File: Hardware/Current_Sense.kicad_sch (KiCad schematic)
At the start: 39 parts, among them IC2 INA241A4IDR, IC3 AMC1350DWVR, J6 Scrut Conn, SW4 Scrut Select, U10 TLV9002QDRQ1, U9 REF35125QDBVR

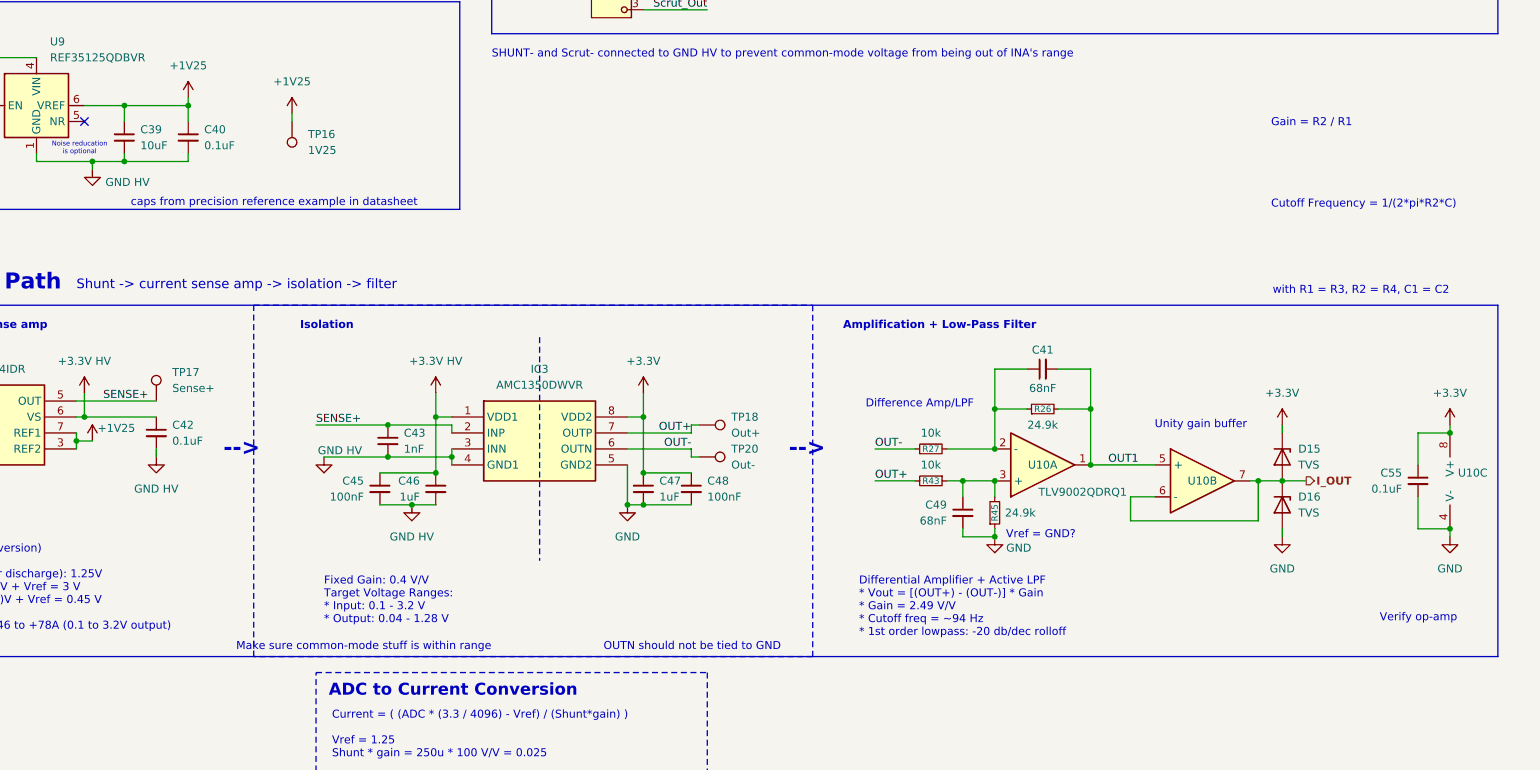
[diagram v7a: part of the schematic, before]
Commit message: refactored and added LPF docs; added fuse, boot_gpio from USB-UART chip
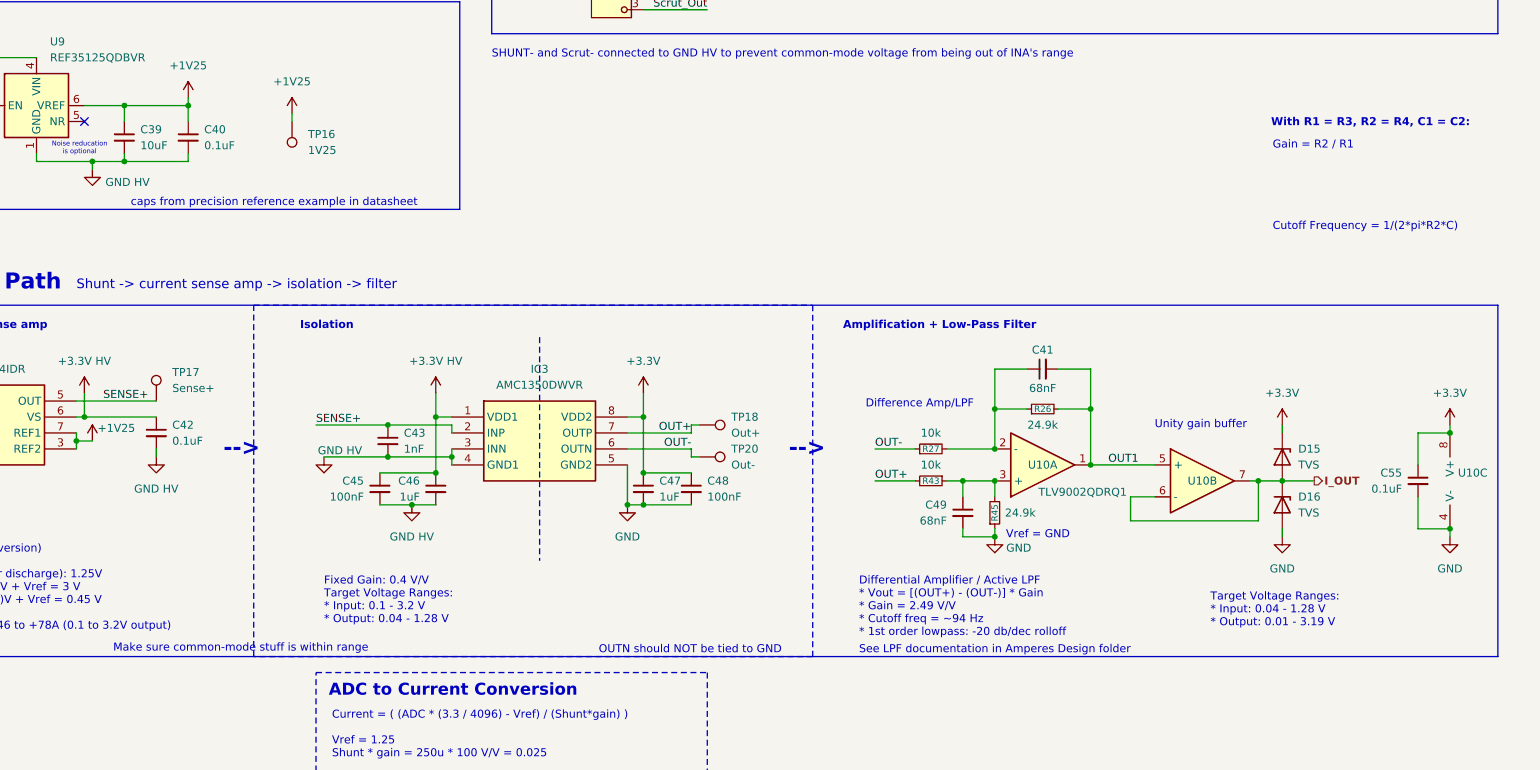
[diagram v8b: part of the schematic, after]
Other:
- note added: "Differential Amplifier / Active LPF * Vout = [(OUT+) - (OUT-)] * Gain * Gain = 2.49 V/V * Cutoff freq = ~94 Hz * 1st order lowpass: -20 db/dec rolloff"
- note added: "OUTN should NOT be tied to GND"
- note added: "See LPF documentation in Amperes Design folder"
- note added: "Target Voltage Ranges: * Input: 0.04 - 1.28 V * Output: 0.01 - 3.19 V"
- note added: "Vref = GND"
- note added: "With R1 = R3, R2 = R4, C1 = C2:"
- note removed: "Differential Amplifier + Active LPF * Vout = [(OUT+) - (OUT-)] * Gain * Gain = 2.49 V/V * Cutoff freq = ~94 Hz * 1st order lowpass: -20 db/dec rolloff"
- note removed: "OUTN should not be tied to GND"
- note removed: "Verify op-amp"
- note removed: "Vref = GND?"
- note removed: "with R1 = R3, R2 = R4, C1 = C2"
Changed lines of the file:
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@@
 		)
 	)
+	(text "Target Voltage Ranges:\n* Input: 0.04 - 1.28 V\n* Output: 0.01 - 3.19 V"
+		(exclude_from_sim no)
+		(at 236.22 152.4 0)
+		(effects
+			(font
+				(size 1.27 1.27)
+			)
+			(justify left top)
+		)
+	)
 	(text "Input"
 		(exclude_from_sim no)
@@
 	(text "Make sure common-mode stuff is within range"
 		(exclude_from_sim no)
-		(at 81.28 160.274 0)
+		(at 61.722 160.528 0)
 		(effects
 			(font
@@
 		)
 	)
-	(text "Verify op-amp"
+	(text "Current = ( (ADC * (3.3 / 4096) - Vref) / (Shunt*gain) )\n\nVref = 1.25\nShunt * gain = 250u * 100 V/V = 0.025\n"
 		(exclude_from_sim no)
-		(at 263.144 155.702 0)
+		(at 96.52 171.196 0)
 		(effects
 			(font
 				(size 1.27 1.27)
-				(color 255 8 29 1)
 			)
 			(justify left top)
 		)
 	)
-	(text "Current = ( (ADC * (3.3 / 4096) - Vref) / (Shunt*gain) )\n\nVref = 1.25\nShunt * gain = 250u * 100 V/V = 0.025\n"
+	(text "Difference Amp/LPF"
 		(exclude_from_sim no)
-		(at 96.52 171.196 0)
+		(at 189.992 122.428 0)
 		(effects
 			(font
 				(size 1.27 1.27)
 			)
-			(justify left top)
 		)
 	)
-	(text "Difference Amp/LPF"
+	(text "Gain: 100 V/V\nRsense = 250 uOhm\nPsense = Rsense * (70A)^2 = 1.225 W\n\nPicked shunt first, then adjusted gain to meet ADC range\nIf additional gain is needed, tweak filter circuit"
 		(exclude_from_sim no)
-		(at 189.992 122.428 0)
+		(at 16.256 183.134 0)
 		(effects
 			(font
 				(size 1.27 1.27)
 			)
+			(justify left top)
 		)
 	)
-	(text "Gain: 100 V/V\nRsense = 250 uOhm\nPsense = Rsense * (70A)^2 = 1.225 W\n\nPicked shunt first, then adjusted gain to meet ADC range\nIf additional gain is needed, tweak filter circuit"
+	(text "See LPF documentation in Amperes Design folder"
 		(exclude_from_sim no)
-		(at 16.256 183.134 0)
+		(at 180.34 160.782 0)
 		(effects
 			(font
 				(size 1.27 1.27)
+				(color 255 8 29 1)
 			)
 			(justify left top)
@@
 		)
 	)
-	(text "with R1 = R3, R2 = R4, C1 = C2"
+	(text "With R1 = R3, R2 = R4, C1 = C2:"
 		(exclude_from_sim no)
-		(at 246.126 103.632 0)
+		(at 245.872 76.962 0)
 		(effects
 			(font
 				(size 1.27 1.27)
+				(thickness 0.254)
+				(bold yes)
 			)
 			(justify left top)
@@
 		)
 	)
-	(text "OUTN should not be tied to GND"
+	(text "OUTN should NOT be tied to GND"
 		(exclude_from_sim no)
-		(at 139.7 160.274 0)
+		(at 138.938 160.782 0)
 		(effects
 			(font
@@
 		)
 	)
-	(text "Differential Amplifier + Active LPF\n* Vout = [(OUT+) - (OUT-)] * Gain\n* Gain = 2.49 V/V\n* Cutoff freq = ~94 Hz\n* 1st order lowpass: -20 db/dec rolloff"
+	(text "Differential Amplifier / Active LPF\n* Vout = [(OUT+) - (OUT-)] * Gain\n* Gain = 2.49 V/V\n* Cutoff freq = ~94 Hz\n* 1st order lowpass: -20 db/dec rolloff"
 		(exclude_from_sim no)
 		(at 180.34 149.86 0)
@@
 	(text "Cutoff Frequency = 1/(2*pi*R2*C)"
 		(exclude_from_sim no)
-		(at 245.872 89.916 0)
+		(at 246.126 93.472 0)
 		(effects
 			(font
@@
 		)
 	)
-	(text "Vref = GND?"
+	(text "Vref = GND"
 		(exclude_from_sim no)
 		(at 203.708 142.494 0)
@@
 	(text "Gain = R2 / R1"
 		(exclude_from_sim no)
-		(at 245.872 76.962 0)
+		(at 246.126 80.518 0)
 		(effects
 			(font
@@
 	(wire
 		(pts
-			(xy 247.65 134.62) (xy 251.46 134.62)
+			(xy 247.65 134.62) (xy 252.73 134.62)
 		)
 		(stroke
@@
 	)
 	(image
-		(at 265.176 96.52)
+		(at 265.43 100.076)
 		(scale 0.860101)
 		(data "iVBORw0KGgoAAAANSUhEUgAAAhUAAACICAYAAABQgxnKAAAABHNCSVQICAgIfAhkiAAAIABJREFU"
@@
 	)
 	(image
-		(at 264.16 83.312)
+		(at 264.414 86.868)
 		(scale 0.844108)
 		(data "iVBORw0KGgoAAAANSUhEUgAAAgMAAAB2CAYAAABVq5AMAAAABHNCSVQICAgIfAhkiAAAF/9JREFU"
@@
 	(hierarchical_label "I_OUT"
 		(shape output)
-		(at 251.46 134.62 0)
+		(at 252.73 134.62 0)
 		(effects
 			(font
